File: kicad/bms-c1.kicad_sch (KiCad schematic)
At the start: 33 parts, among them J1 MicroFit 2x12, J2 B4B-PH-SM4, J3 USB_B_Micro, J4 B3B-PH-SM4, J5 B2B-PH-SM4, J6 B4B-PH-SM4, P1 CONN_01X01, P2 CONN_01X01, P3 CONN_01X01, P4 CONN_01X01, P5 CONN_01X01

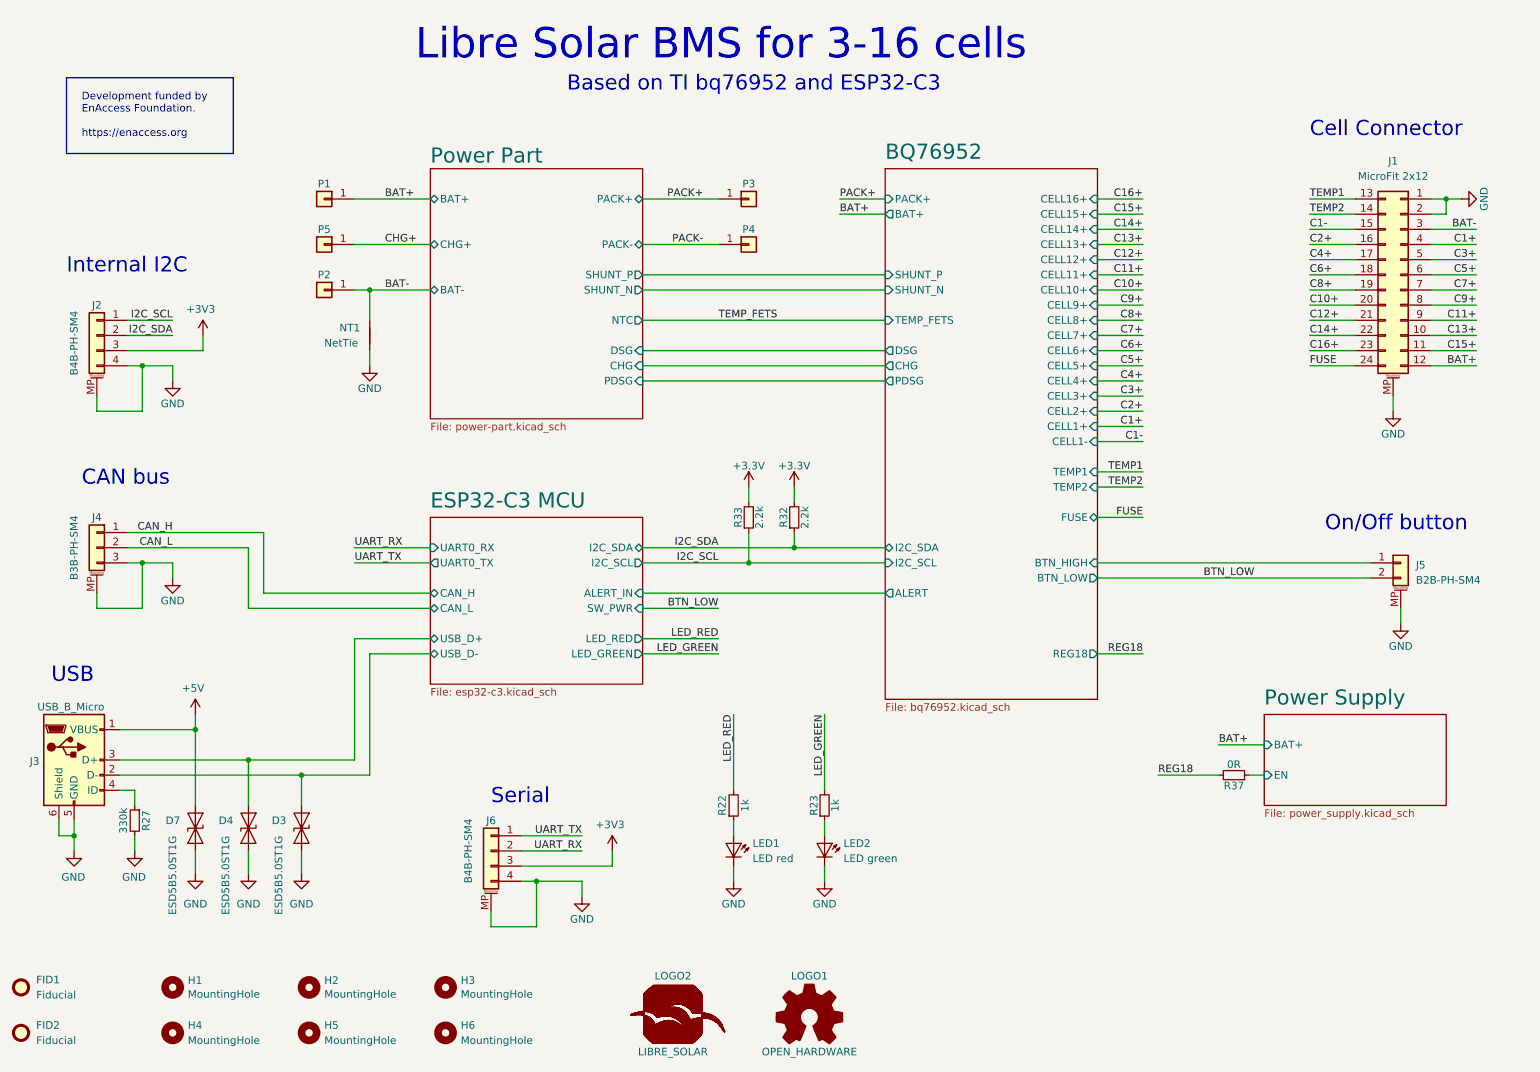
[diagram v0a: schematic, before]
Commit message: v0.4.0: Multiple improvements for new board revision
- Use LMR38010 for internal power supply (max. 80V instead of 60V)
- Change USB connector from Micro-A to C and remove 5V power supply
  which was not working anyway. The board cannot be powered by USB
  only.
- Add TS2 (connected to DFETOFF) to measure shunt temperature
- Add RS-485 transceiver (sharing the connector with CAN)
- Switch I2C pins of ESP32-C3 to GPIO8/9. This allows to re-use the
  I2C pull-ups for strapping configuration and frees two pins for the
  RS-485 transceiver RE and DE pins. Also we may get rid of the I2C
  glitches during start-up.
- Reduce DSG gate resistor R57 to 47R to increase switch-off speed.
- Use more easily available and cheaper Würth 7466005R terminals with
  countersunk hole/thread.
- Adjust some resistors to reduce number of different parts
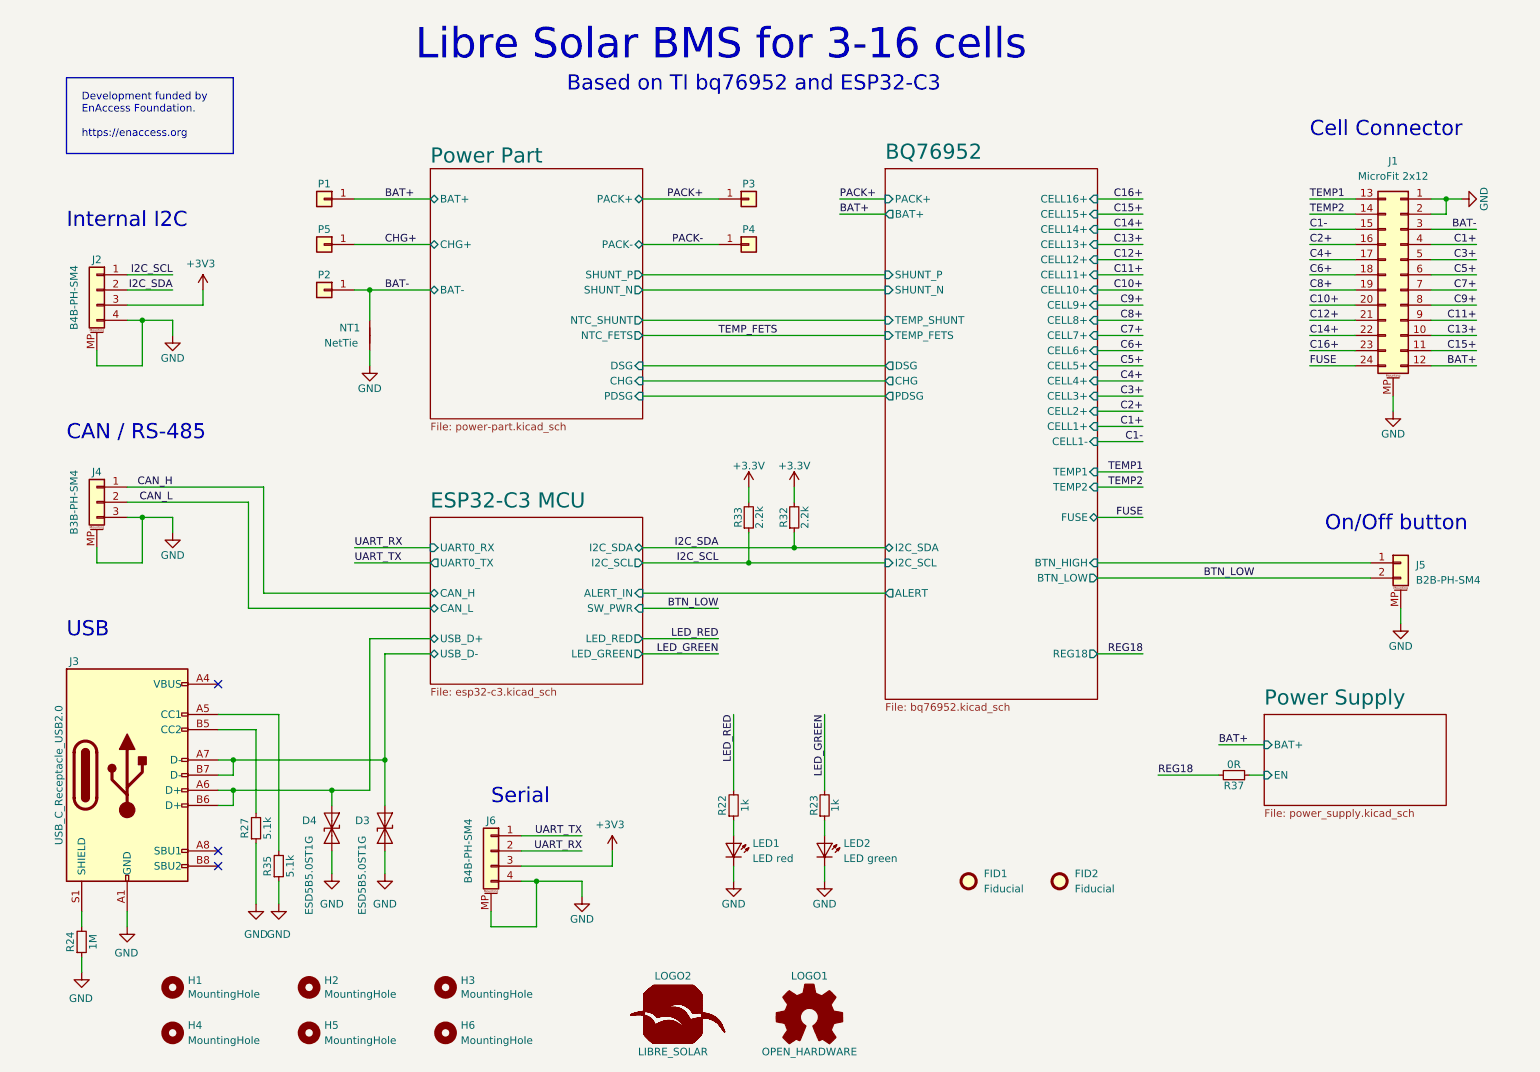
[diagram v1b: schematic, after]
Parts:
- removed D7: ESD5B5.0ST1G, LibreSolar:D_SOD-523, symbol Diode:SZESD9B5.0ST5G
- removed J3: USB_B_Micro, LibreSolar:USB_Micro-B_10103594-0001LF, symbol Connector:USB_B_Micro
- added J3: USB_C_Receptacle_USB2.0, Connector_USB:USB_C_Receptacle_GCT_USB4105-xx-A_16P_TopMnt_Horizontal, symbol Connector:USB_C_Receptacle_USB2.0
- added R24: 1M, LibreSolar:R_0603_1608, symbol LibreSolar:R
- added R35: 5.1k, LibreSolar:R_0603_1608, symbol LibreSolar:R
- J1: Manufacturer Molex -> Würth; PartNumber 43045-1810 -> 662024231722; Remarks Alternative: Würth 662024231722, mating connector: 66202411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 -> Mating connector: 662024113322
- P1, P2, P3, P4: footprint LibreSolar:Wuerth_PowerOne_SMD_LF990005 -> LibreSolar:Wuerth_WP-SMBU_7466005R; PartNumber LF990005 -> 7466005R; Remarks Alternative: Erni 225852 -> Alternative: Erni 225858
- R27: value 330k -> 5.1k
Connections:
- net ESP32-C3 MCU/USB_D+: now also J3.A6 (D+), J3.B6 (D+)
- net ESP32-C3 MCU/USB_D-: now also J3.A7 (D-), J3.B7 (D-)
- net GND: now also R27.1, J3.A1 (GND), J3.A12 (GND), J3.B1 (GND), J3.B12 (GND), R24.1, R35.1; no longer R27.2
- new net: J3.S1 (SHIELD), R24.2
- new net: J3.B5 (CC2), R27.2
- new net: J3.A5 (CC1), R35.2
- new net: J3.A4 (VBUS), J3.A9 (VBUS), J3.B4 (VBUS), J3.B9 (VBUS)
- no-connect marks 0 -> 3
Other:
- sheet BQ76952 ports: added TEMP_SHUNT; removed none
- sheet Power Part ports: added NTC_FETS, NTC_SHUNT; removed NTC
- note added: "CAN / RS-485"
- note removed: "CAN bus"
- moved on the sheet: D3, D4, FID1, FID2, J2, J4
